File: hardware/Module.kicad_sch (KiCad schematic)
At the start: 119 parts, among them J1 Jack, J10 Jack, J11 Jack, J12 Jack, J13 Micro_SD, J14 NW_B, J15 Jack, J16 Jack, J17 Power, J18 Jack, J19 Jack, J2 OLED, J20 SW_B, J21 NW_A, J22 SW_A, J23 NE_A, J3 NE_B, J4 Jack, J5 Jack, J6 Jack, J7 Jack, J8 Jack, J9 Jack, SW1 Encoder, U1 TL074, U2 TL074, U3 TL074, U4 MCP6004, U5 MCP6002, U7 LM4040C10

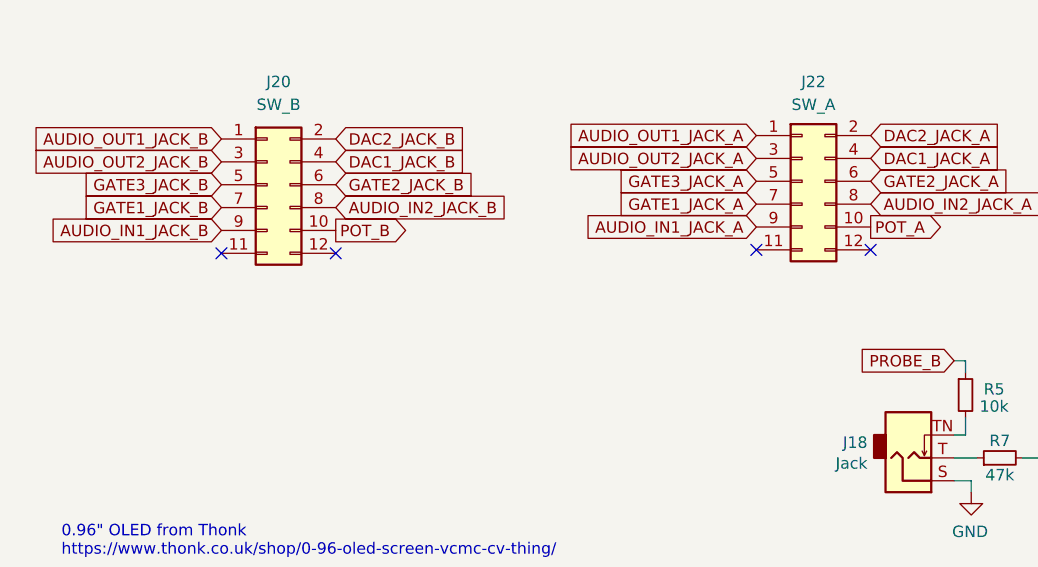
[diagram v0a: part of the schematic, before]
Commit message: Fix all DRC checks
Signed-off-by: Petr Horacek <hrck@protonmail.com>
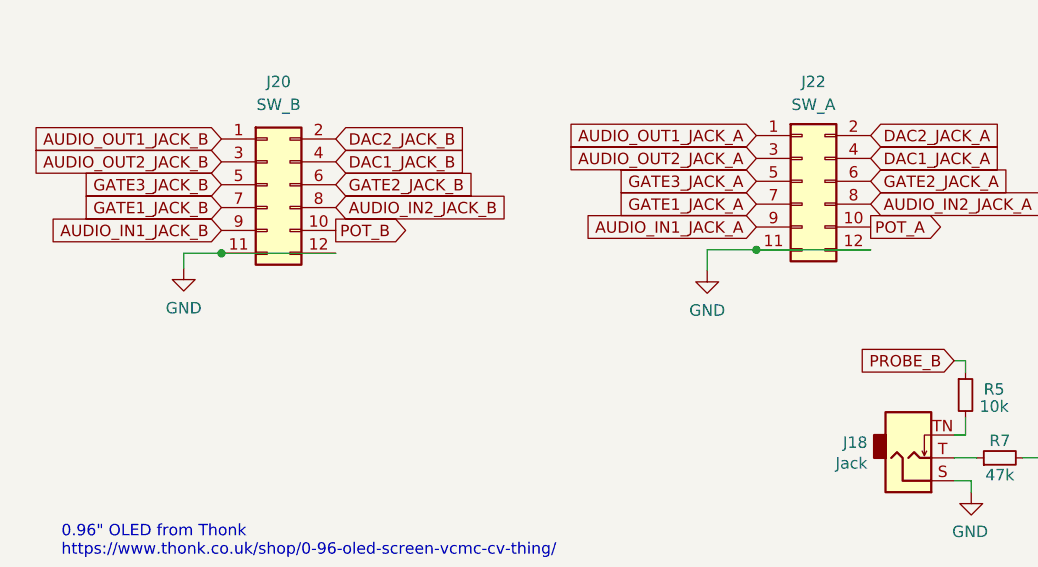
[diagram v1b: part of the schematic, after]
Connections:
- net GND: now also J20.11 (Pin_11), J20.12 (Pin_12), J22.11 (Pin_11), J22.12 (Pin_12)
- no-connect marks 26 -> 22
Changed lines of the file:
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@@
   (junction (at 344.17 229.997) (diameter 0) (color 0 0 0 0)
   )
+  (junction (at 94.234 214.249) (diameter 0) (color 0 0 0 0)
+  )
   (junction (at 386.08 229.997) (diameter 0) (color 0 0 0 0)
   )
@@
   (junction (at 304.038 120.015) (diameter 0) (color 0 0 0 0)
   )
+  (junction (at 34.798 214.63) (diameter 0) (color 0 0 0 0)
+  )
   (junction (at 340.36 33.147) (diameter 0) (color 0 0 0 0)
   )
@@
   (no_connect (at 218.44 94.869))
   (no_connect (at 373.38 205.867))
-  (no_connect (at 34.798 214.63))
-  (no_connect (at 47.498 214.63))
-  (no_connect (at 94.234 214.249))
-  (no_connect (at 106.934 214.249))
   (no_connect (at 106.553 143.764))
   (no_connect (at 93.853 143.764))
@@
     (stroke (width 0) (type default) (color 0 0 0 0))
   )
+  (wire (pts (xy 34.798 214.63) (xy 47.498 214.63))
+    (stroke (width 0) (type default) (color 0 0 0 0))
+  )
   (wire (pts (xy 238.76 105.664) (xy 238.76 106.934))
     (stroke (width 0) (type default) (color 0 0 0 0))
@@
     (stroke (width 0) (type default) (color 0 0 0 0))
   )
+  (wire (pts (xy 88.773 214.249) (xy 94.234 214.249))
+    (stroke (width 0) (type default) (color 0 0 0 0))
+  )
   (wire (pts (xy 147.32 241.046) (xy 147.32 239.776))
     (stroke (width 0) (type default) (color 0 0 0 0))
@@
     (stroke (width 0) (type default) (color 0 0 0 0))
   )
+  (wire (pts (xy 94.234 214.249) (xy 106.934 214.249))
+    (stroke (width 0) (type default) (color 0 0 0 0))
+  )
   (wire (pts (xy 365.125 160.147) (xy 371.475 160.147))
     (stroke (width 0) (type default) (color 0 0 0 0))
@@
     (stroke (width 0) (type default) (color 0 0 0 0))
   )
+  (wire (pts (xy 88.773 214.249) (xy 88.773 216.535))
+    (stroke (width 0) (type default) (color 0 0 0 0))
+  )
   (wire (pts (xy 234.315 62.357) (xy 257.81 62.357))
     (stroke (width 0) (type default) (color 0 0 0 0))
@@
     (stroke (width 0) (type default) (color 0 0 0 0))
   )
+  (wire (pts (xy 30.607 214.63) (xy 30.607 216.281))
+    (stroke (width 0) (type default) (color 0 0 0 0))
+  )
   (wire (pts (xy 217.932 260.223) (xy 210.312 260.223))
     (stroke (width 0) (type default) (color 0 0 0 0))
@@
     (stroke (width 0) (type default) (color 0 0 0 0))
   )
+  (wire (pts (xy 34.798 214.63) (xy 30.607 214.63))
+    (stroke (width 0) (type default) (color 0 0 0 0))
+  )
   (wire (pts (xy 40.64 266.827) (xy 57.15 266.827))
     (stroke (width 0) (type default) (color 0 0 0 0))
@@
     (pin "2")
   )
+  (symbol (lib_id "power:GND") (at 30.607 216.281 0) (unit 1)
+    (in_bom yes) (on_board yes)
+    (property "Reference" "#PWR?" (id 0) (at 30.607 222.631 0)
+      (effects (font (size 1.27 1.27)) hide)
+    )
+    (property "Value" "GND" (id 1) (at 30.607 220.726 0))
+    (property "Footprint" "" (id 2) (at 30.607 216.281 0)
+      (effects (font (size 1.27 1.27)) hide)
+    )
+    (property "Datasheet" "" (id 3) (at 30.607 216.281 0)
+      (effects (font (size 1.27 1.27)) hide)
+    )
+    (pin "1")
+  )
   (symbol (lib_id "Connector:AudioJack2_SwitchT") (at 196.85 152.654 180) (unit 1)
     (in_bom yes) (on_board yes)
@@
     (pin "S2")
   )
+  (symbol (lib_id "power:GND") (at 88.773 216.535 0) (unit 1)
+    (in_bom yes) (on_board yes)
+    (property "Reference" "#PWR?" (id 0) (at 88.773 222.885 0)
+      (effects (font (size 1.27 1.27)) hide)
+    )
+    (property "Value" "GND" (id 1) (at 88.773 220.98 0))
+    (property "Footprint" "" (id 2) (at 88.773 216.535 0)
+      (effects (font (size 1.27 1.27)) hide)
+    )
+    (property "Datasheet" "" (id 3) (at 88.773 216.535 0)
+      (effects (font (size 1.27 1.27)) hide)
+    )
+    (pin "1")
+  )
   (symbol (lib_id "Device:FerriteBead_Small") (at 358.14 28.067 90) (unit 1)
     (in_bom yes) (on_board yes)
@@
       (reference "#PWR0104") (unit 1) (value "+3.3VA") (footprint "")
     )
+    (path "/36c52104-9383-4fec-93e5-771b8c41ab2c"
+      (reference "#PWR?") (unit 1) (value "GND") (footprint "")
+    )
+    (path "/56dbafc3-2b76-42f6-81d5-b8e8ad40462e"
+      (reference "#PWR?") (unit 1) (value "GND") (footprint "")
+    )
     (path "/00000000-0000-0000-0000-000062372793"

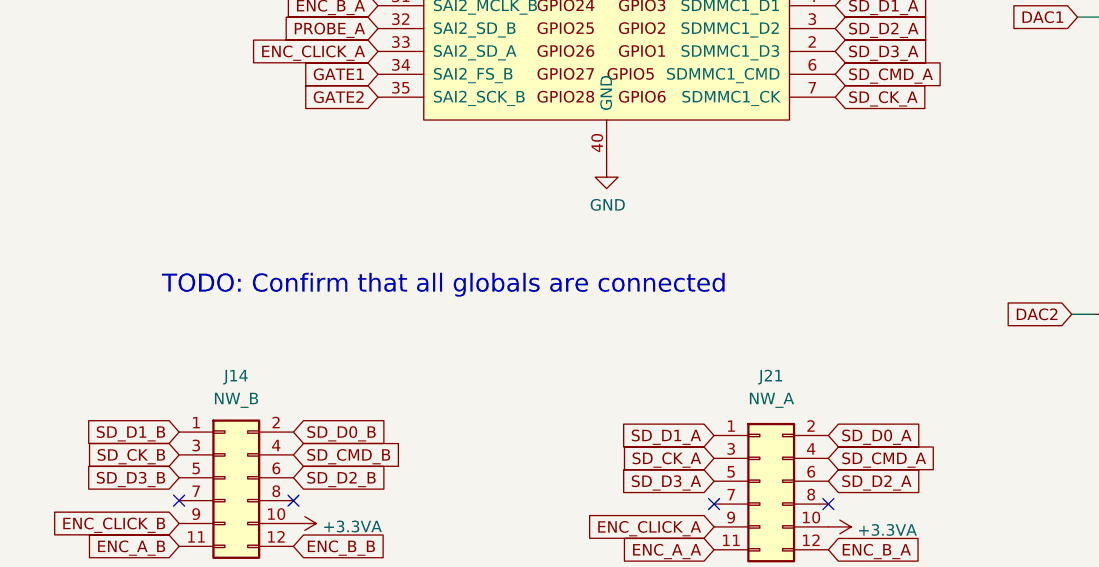
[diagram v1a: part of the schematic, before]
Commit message: Fix mousebites
Signed-off-by: Petr Horacek <hrck@protonmail.com>
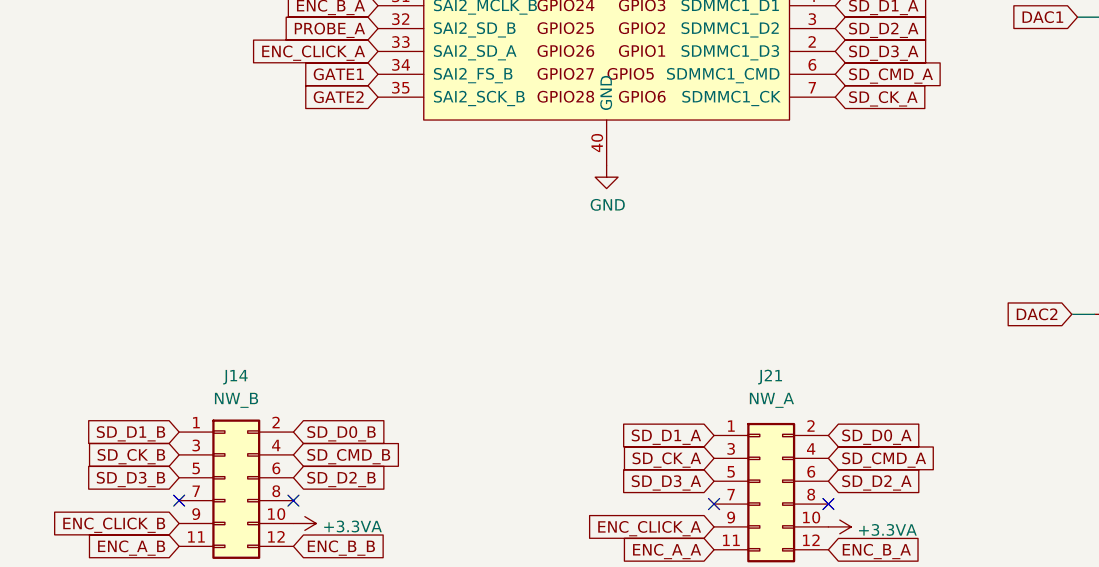
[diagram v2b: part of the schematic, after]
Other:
- note removed: "TODO: Confirm that all globals are connected"
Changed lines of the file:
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@@
     (effects (font (size 1.27 1.27)) (justify left bottom))
   )
-  (text "TODO: Confirm that all globals are connected" (at 32.512 120.65 0)
-    (effects (font (size 2.0066 2.0066)) (justify left bottom))
-  )
   (text "RES" (at 63.373 259.715 0)
     (effects (font (size 1.27 1.27)) (justify left bottom))
@@
   (symbol (lib_id "power:GND") (at 30.607 216.281 0) (unit 1)
     (in_bom yes) (on_board yes)
-    (property "Reference" "#PWR?" (id 0) (at 30.607 222.631 0)
+    (property "Reference" "#PWR0106" (id 0) (at 30.607 222.631 0)
       (effects (font (size 1.27 1.27)) hide)
     )
@@
   (symbol (lib_id "power:GND") (at 88.773 216.535 0) (unit 1)
     (in_bom yes) (on_board yes)
-    (property "Reference" "#PWR?" (id 0) (at 88.773 222.885 0)
+    (property "Reference" "#PWR0105" (id 0) (at 88.773 222.885 0)
       (effects (font (size 1.27 1.27)) hide)
     )
@@
       (reference "#PWR0104") (unit 1) (value "+3.3VA") (footprint "")
     )
-    (path "/36c52104-9383-4fec-93e5-771b8c41ab2c"
-      (reference "#PWR?") (unit 1) (value "GND") (footprint "")
-    )
     (path "/56dbafc3-2b76-42f6-81d5-b8e8ad40462e"
-      (reference "#PWR?") (unit 1) (value "GND") (footprint "")
+      (reference "#PWR0105") (unit 1) (value "GND") (footprint "")
+    )
+    (path "/36c52104-9383-4fec-93e5-771b8c41ab2c"
+      (reference "#PWR0106") (unit 1) (value "GND") (footprint "")
     )
     (path "/00000000-0000-0000-0000-000062372793"
